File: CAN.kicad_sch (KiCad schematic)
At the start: 8 parts, among them U103 SN65HVD230DR

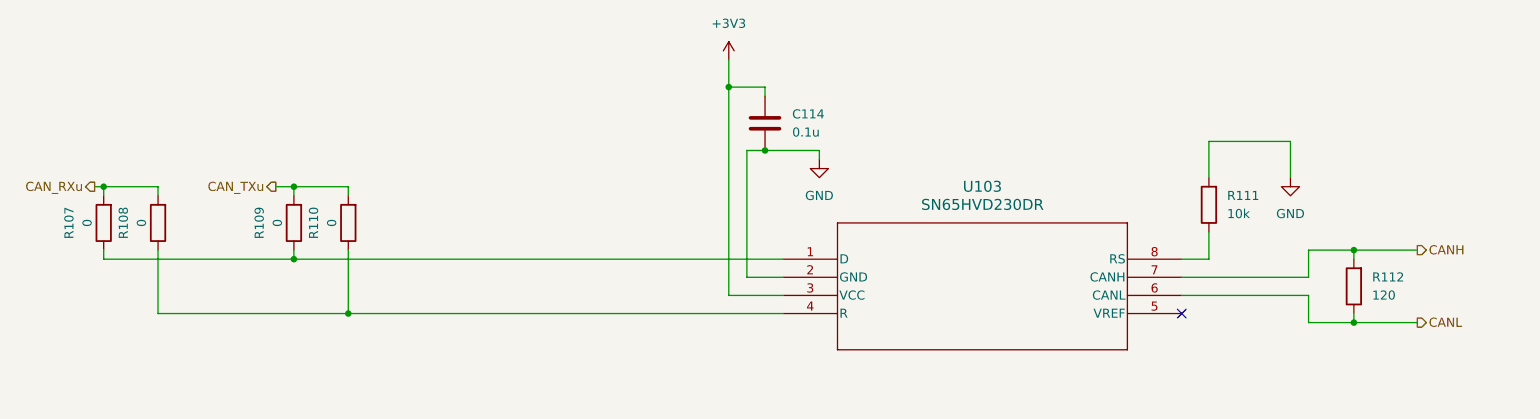
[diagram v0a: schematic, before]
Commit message: Added gyro, current sense, removed servo control, added temp sense
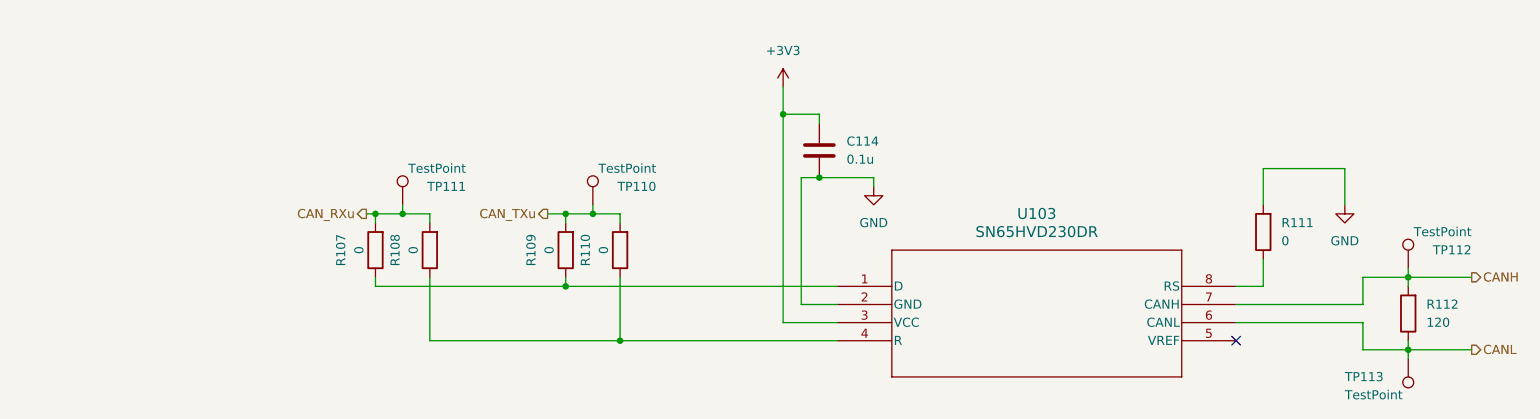
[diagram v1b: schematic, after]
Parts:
- added TP110, TP111, TP112, TP113: TestPoint, TestPoint:TestPoint_Pad_D2.0mm, symbol Connector:TestPoint
- R111: value 10k -> 0
- U103: footprint SN65HVD230DR:D8 -> D8
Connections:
- net CANH: now also TP112.1
- net CANL: now also TP113.1
- net CAN_RXu: now also TP111.1
- net CAN_TXu: now also TP110.1
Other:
- moved on the sheet: C114, R107, R108, R109, R110, R111, R112, U103

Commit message: finished up schematic, added magnetic sensor, cleaned up pins, etc.
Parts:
- C114: footprint Capacitor_SMD:C_0805_2012Metric_Pad1.18x1.45mm_HandSolder -> Capacitor_SMD:C_0603_1608Metric_Pad1.08x0.95mm_HandSolder; Digikey https://www.digikey.com/en/products/detail/murata-electroni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 -> (none)
- TP110, TP111, TP112, TP113: footprint TestPoint:TestPoint_Pad_D2.0mm -> TestPoint:TestPoint_Pad_D1.0mm
- U103: Digikey https://www.digikey.com/en/products/detail/texas-instrument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 -> (none)
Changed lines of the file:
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@@
 			)
 		)
-		(property "Footprint" "TestPoint:TestPoint_Pad_D2.0mm"
+		(property "Footprint" "TestPoint:TestPoint_Pad_D1.0mm"
 			(at 201.93 106.68 0)
 			(effects
@@
 			)
 		)
-		(property "Digikey" "https://www.digikey.com/en/products/detail/texas-instruments/SN65HVD230DR/404367"
-			(at 127 96.52 0)
-			(effects
-				(font
-					(size 1.27 1.27)
-				)
-				(hide yes)
-			)
-		)
 		(pin "3"
 		)
@@
 			)
 		)
-		(property "Footprint" "Capacitor_SMD:C_0805_2012Metric_Pad1.18x1.45mm_HandSolder"
+		(property "Footprint" "Capacitor_SMD:C_0603_1608Metric_Pad1.08x0.95mm_HandSolder"
 			(at 125.4252 81.28 0)
 			(effects
@@
 			)
 		)
-		(property "Digikey" "https://www.digikey.com/en/products/detail/murata-electronics/GCM21BR72A104KA37L/1641663"
-			(at 124.46 77.47 0)
-			(effects
-				(font
-					(size 1.27 1.27)
-				)
-				(hide yes)
-			)
-		)
 		(pin "2"
 		)
@@
 			)
 		)
-		(property "Footprint" "TestPoint:TestPoint_Pad_D2.0mm"
+		(property "Footprint" "TestPoint:TestPoint_Pad_D1.0mm"
 			(at 71.12 85.09 0)
 			(effects
@@
 			)
 		)
-		(property "Footprint" "TestPoint:TestPoint_Pad_D2.0mm"
+		(property "Footprint" "TestPoint:TestPoint_Pad_D1.0mm"
 			(at 97.79 85.09 0)
 			(effects
@@
 			)
 		)
-		(property "Footprint" "TestPoint:TestPoint_Pad_D2.0mm"
+		(property "Footprint" "TestPoint:TestPoint_Pad_D1.0mm"
 			(at 212.09 93.98 0)
 			(effects

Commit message: cleaned up refdes
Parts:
- removed TP112, TP113: TestPoint, TestPoint:TestPoint_Pad_D1.0mm, symbol Connector:TestPoint
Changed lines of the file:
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@@
-	(wire
-		(pts
-			(xy 207.01 93.98) (xy 207.01 95.25)
-		)
-		(stroke
-			(width 0)
-			(type default)
-		)
-	)
 	(wire
 		(pts
@@
 		(pts
 			(xy 124.46 73.66) (xy 124.46 72.39)
-		)
-		(stroke
-			(width 0)
-			(type default)
-		)
-	)
-	(wire
-		(pts
-			(xy 207.01 105.41) (xy 207.01 106.68)
 		)
 		(stroke
@@
 	)
 	(symbol
-		(lib_id "Connector:TestPoint")
-		(at 207.01 106.68 180)
-		(unit 1)
-		(exclude_from_sim no)
-		(in_bom yes)
-		(on_board yes)
-		(dnp no)
-		(property "Reference" "TP113"
-			(at 198.12 109.22 0)
-			(effects
-				(font
-					(size 1.27 1.27)
-				)
-				(justify right)
-			)
-		)
-		(property "Value" "TestPoint"
-			(at 198.12 111.76 0)
-			(effects
-				(font
-					(size 1.27 1.27)
-				)
-				(justify right)
-			)
-		)
-		(property "Footprint" "TestPoint:TestPoint_Pad_D1.0mm"
-			(at 201.93 106.68 0)
-			(effects
-				(font
-					(size 1.27 1.27)
-				)
-				(hide yes)
-			)
-		)
-		(property "Datasheet" "~"
-			(at 201.93 106.68 0)
-			(effects
-				(font
-					(size 1.27 1.27)
-				)
-				(hide yes)
-			)
-		)
-		(property "Description" "test point"
-			(at 207.01 106.68 0)
-			(effects
-				(font
-					(size 1.27 1.27)
-				)
-				(hide yes)
-			)
-		)
-		(pin "1"
-		)
-		(instances
-			(project "TeensyDAQ_REV0"
-				(path "/11737956-c422-45b5-a9a0-ee63a853502c/0f2f77fc-00e9-40fa-a5cc-7ba39dc1577b"
-					(reference "TP113")
-					(unit 1)
-				)
-			)
-		)
-	)
-	(symbol
 		(lib_id "SN65HVD230DR:SN65HVD230DR")
 		(at 127 96.52 0)
@@
 					(unit 1)
 				)
-			)
-		)
-	)
-	(symbol
-		(lib_id "Connector:TestPoint")
-		(at 207.01 93.98 0)
-		(unit 1)
-		(exclude_from_sim no)
-		(in_bom yes)
-		(on_board yes)
-		(dnp no)
-		(property "Reference" "TP112"
-			(at 215.9 91.44 0)
-			(effects
-				(font
-					(size 1.27 1.27)
-				)
-				(justify right)
-			)
-		)
-		(property "Value" "TestPoint"
-			(at 215.9 88.9 0)
-			(effects
-				(font
-					(size 1.27 1.27)
-				)
-				(justify right)
-			)
-		)
-		(property "Footprint" "TestPoint:TestPoint_Pad_D1.0mm"
-			(at 212.09 93.98 0)
-			(effects
-				(font
-					(size 1.27 1.27)
-				)
-				(hide yes)
-			)
-		)
-		(property "Datasheet" "~"
-			(at 212.09 93.98 0)
-			(effects
-				(font
-					(size 1.27 1.27)
-				)
-				(hide yes)
-			)
-		)
-		(property "Description" "test point"
-			(at 207.01 93.98 0)
-			(effects
-				(font
-					(size 1.27 1.27)
-				)
-				(hide yes)
-			)
-		)
-		(pin "1"
-		)
-		(instances
-			(project "TeensyDAQ_REV0"
-				(path "/11737956-c422-45b5-a9a0-ee63a853502c/0f2f77fc-00e9-40fa-a5cc-7ba39dc1577b"
-					(reference "TP112")
-					(unit 1)
-				)

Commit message: removed a VDIV input and changed it to a thermistor input. Re-ran fabrication output
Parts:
- renumbered TP111 to RX100, TP110 to TX100
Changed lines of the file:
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@@
 		(on_board yes)
 		(dnp no)
-		(property "Reference" "TP111"
+		(property "Reference" "RX100"
 			(at 74.93 82.55 0)
 			(effects
@@
 			(project "TeensyDAQ_REV0"
 				(path "/11737956-c422-45b5-a9a0-ee63a853502c/0f2f77fc-00e9-40fa-a5cc-7ba39dc1577b"
-					(reference "TP111")
+					(reference "RX100")
 					(unit 1)
 				)
@@
 		(on_board yes)
 		(dnp no)
-		(property "Reference" "TP110"
+		(property "Reference" "TX100"
 			(at 101.6 82.55 0)
 			(effects
@@
 			(project "TeensyDAQ_REV0"
 				(path "/11737956-c422-45b5-a9a0-ee63a853502c/0f2f77fc-00e9-40fa-a5cc-7ba39dc1577b"
-					(reference "TP110")
+					(reference "TX100")
 					(unit 1)
 				)

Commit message: added TVS diodes to external pins for protection. Ran fabrication output. Ran iBOM generation. All part links can be seen in the iBOM. Download and open to see this
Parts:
- C114: DIGIKEY LINK (none) -> https://www.digikey.com/en/products/detail/murata-electroni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
- R107, R108, R109, R110, R111: DIGIKEY LINK (none) -> https://www.digikey.com/en/products/detail/yageo/RC0603JR-0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
- R112: DIGIKEY LINK (none) -> https://www.digikey.com/en/products/detail/yageo/RC0603FR-0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
- U103: DIGIKEY LINK (none) -> https://www.digikey.com/en/products/detail/texas-instrument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
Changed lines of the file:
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@@
 	(generator_version "8.0")
 	(paper "A4")
+	(title_block
+		(date "2025-02-11")
+	)
 	(junction
 		(at 119.38 72.39)
@@
 		)
 		(property "Description" "Resistor"
+			(at 96.52 91.44 0)
+			(effects
+				(font
+					(size 1.27 1.27)
+				)
+				(hide yes)
+			)
+		)
+		(property "DIGIKEY LINK" "https://www.digikey.com/en/products/detail/yageo/RC0603JR-070RL/726675"
 			(at 96.52 91.44 0)
 			(effects
@@
 			)
 		)
+		(property "DIGIKEY LINK" "https://www.digikey.com/en/products/detail/texas-instruments/SN65HVD230DR/404367"
+			(at 127 96.52 0)
+			(effects
+				(font
+					(size 1.27 1.27)
+				)
+				(hide yes)
+			)
+		)
 		(pin "3"
 		)
@@
 			)
 		)
+		(property "DIGIKEY LINK" "https://www.digikey.com/en/products/detail/yageo/RC0603FR-07120RL/726920"
+			(at 207.01 100.33 0)
+			(effects
+				(font
+					(size 1.27 1.27)
+				)
+				(hide yes)
+			)
+		)
 		(pin "2"
 		)
@@
 			)
 		)
+		(property "DIGIKEY LINK" "https://www.digikey.com/en/products/detail/yageo/RC0603JR-070RL/726675"
+			(at 62.23 91.44 0)
+			(effects
+				(font
+					(size 1.27 1.27)
+				)
+				(hide yes)
+			)
+		)
 		(pin "2"
 		)
@@
 			)
 		)
+		(property "DIGIKEY LINK" "https://www.digikey.com/en/products/detail/yageo/RC0603JR-070RL/726675"
+			(at 186.69 88.9 0)
+			(effects
+				(font
+					(size 1.27 1.27)
+				)
+				(hide yes)
+			)
+		)
 		(pin "2"
 		)
@@
 			)
 		)
+		(property "DIGIKEY LINK" "https://www.digikey.com/en/products/detail/murata-electronics/GCJ188R71E104KA12D/7363221"
+			(at 124.46 77.47 0)
+			(effects
+				(font
+					(size 1.27 1.27)
+				)
+				(hide yes)
+			)
+		)
 		(pin "2"
 		)
@@
 			)
 		)
+		(property "DIGIKEY LINK" "https://www.digikey.com/en/products/detail/yageo/RC0603JR-070RL/726675"
+			(at 88.9 91.44 0)
+			(effects
+				(font
+					(size 1.27 1.27)
+				)
+				(hide yes)
+			)
+		)
 		(pin "2"
 		)
@@
 			(at 69.85 91.44 0)
 			(effects
+				(font
+					(size 1.27 1.27)
+				)
+				(hide yes)
+			)
+		)
+		(property "DIGIKEY LINK" "https://www.digikey.com/en/products/detail/yageo/RC0603JR-070RL/726675"
+			(at 69.85 91.44 0)
+			(effects
